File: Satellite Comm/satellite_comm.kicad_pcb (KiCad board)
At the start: 2 copper layers, 139.7 x 100.3 mm, 9 parts, among them J1 PC104_40Pin_2.54mm, J2 RockBLOCK9603, U1 SAM-M8Q

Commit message: Deleted all caches and renamed files...
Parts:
- removed J2: RockBLOCK9603, Molex_533981071:Molex_53398-1071
- removed U1: SAM-M8Q, SAMM8Q:SAM-M8Q
- removed XB1: XBee, WhitworthStandard:xbee-standard
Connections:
- J1 pad 1: GND -> +5V
- J1 pad 10: /I2C_SCL -> /IRIDIUM_NET_AVAIL
- J1 pad 11: /I2C_SDA -> GNDS
- J1 pad 12: GNDS -> /POD_RX
- J1 pad 13: /DIO1 -> /POD_TX
- J1 pad 14: /SPI_CLK -> /POD_WAKE
- J1 pad 15: /SPI_MISO -> /A3
- J1 pad 16: /SPI_MOSI -> /A4
- J1 pad 17: GND -> GNDPWR
- J1 pad 19: +3V3 -> +BATT
- J1 pad 2: /EXT_TEMP -> /SPI_MOSI
- J1 pad 20: GND -> +3V3
- J1 pad 21: +3V3 -> GND
- J1 pad 22: +3V3 -> +BATT
- J1 pad 24: /RADIO_WAKE -> /LED_A
- J1 pad 25: /1_WIRE -> /LED_B
- J1 pad 26: /IRIDIUM_NET_AVAIL -> /LED_C
- J1 pad 27: /IRIDIUM_TX -> /A0
- J1 pad 28: /IRIDIUM_RX -> /A1
- J1 pad 29: /IRIDIUM_PWR_CTRL -> /A2
- J1 pad 3: /A3 -> /SPI_MISO
- J1 pad 30: /INTERBOARD_0 -> /AUDIO_ALERT
- J1 pad 31: /INTERBOARD_1 -> /PWM
- J1 pad 32: /INTERBOARD_2 -> /DIO1
- J1 pad 33: /INTERBOARD_3 -> /INTERBOARD_0
- J1 pad 34: /PWM -> /RADIO_TX
- J1 pad 35: /LED_C -> /RADIO_RX
- J1 pad 36: /LED_B -> /RADIO_WAKE
- J1 pad 37: /LED_A -> /I2C_SDA
- J1 pad 38: /RADIO_RX -> /BT_RX
- J1 pad 39: /RADIO_TX -> /BT_TX
- J1 pad 4: /A2 -> /SPI_CLK
- J1 pad 40: +5V -> GND
- J1 pad 5: /A1 -> /I2C_SCL
- J1 pad 6: /A0 -> /DIO2
- J1 pad 7: /POD_WAKE -> /IRIDIUM_PWR_CTRL
- J1 pad 8: /POD_TX -> /IRIDIUM_RX
- J1 pad 9: /POD_RX -> /IRIDIUM_TX
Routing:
- net GND: track 0.00 -> 277.1 mm
- net +BATT: track 0.00 -> 2.54 mm
- net +3V3: track 2.54 -> 0.00 mm
- added copper zone on B.Cu, net GND
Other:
- board text added: "High Altitude Balloon Command Module 2.0 Processing Board"
- board text removed: "High Altitude Balloon Command Module 2.1 Processing Board"

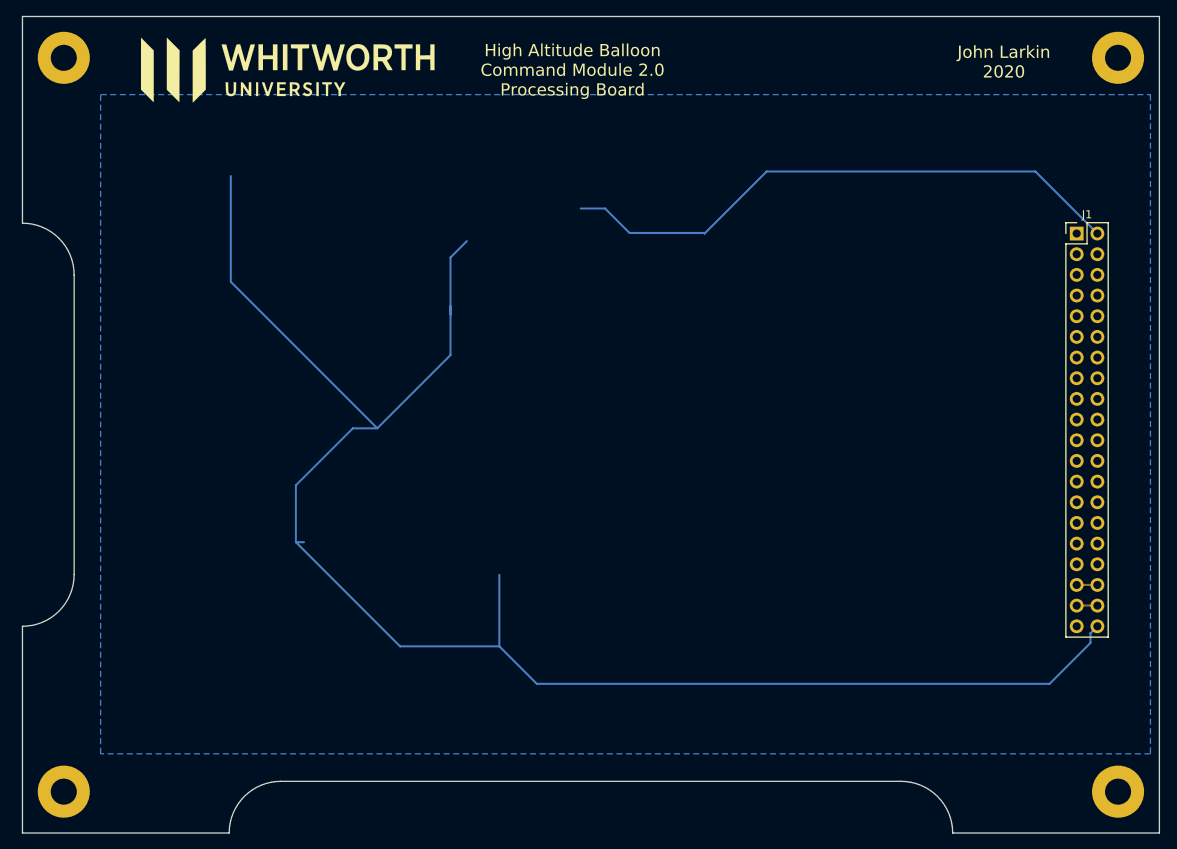
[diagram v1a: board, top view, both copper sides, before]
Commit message: silks are not very clean, laid out components, added front ground plane
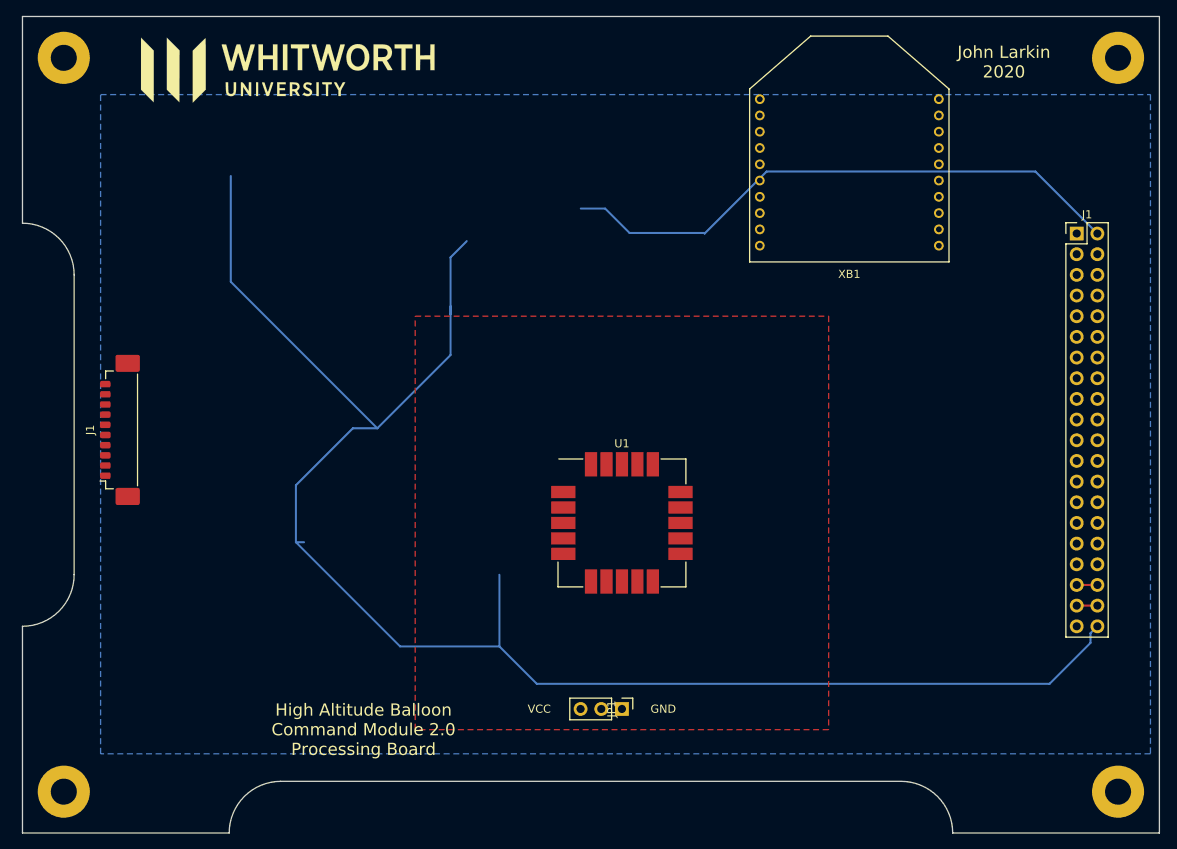
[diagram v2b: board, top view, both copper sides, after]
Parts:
- added J1: RockBlock Connector, Connector_Molex:Molex_PicoBlade_53398-1071_1x10-1MP_P1.25mm_Vertical, F.Cu at (36.8, 76.2)
- added JP1: Jumper_3_Open, Connector_PinHeader_2.54mm:PinHeader_1x03_P2.54mm_Vertical, F.Cu at (99.1, 110.5)
- added U1: SAM-M8Q, RF_GPS:ublox_SAM-M8Q_HandSolder, F.Cu at (99.1, 87.6)
- added XB1: XBee, WhitworthStandard:xbee-standard, F.Cu at (127.0, 35.6)
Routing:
- added copper zone on F.Cu, net GND
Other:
- board text added: "GND"
- board text added: "VCC"

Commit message: started working on tracks
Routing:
- net GND: track 277.1 -> 32.3 mm
- net +3V3: track 0.00 -> 187.4 mm, vias 0 -> 3
- net Net-(JP1-Pad2): track 0.00 -> 47.4 mm, vias 0 -> 1
- removed copper zone on B.Cu, net GND
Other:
- board text added: "Pin 1"

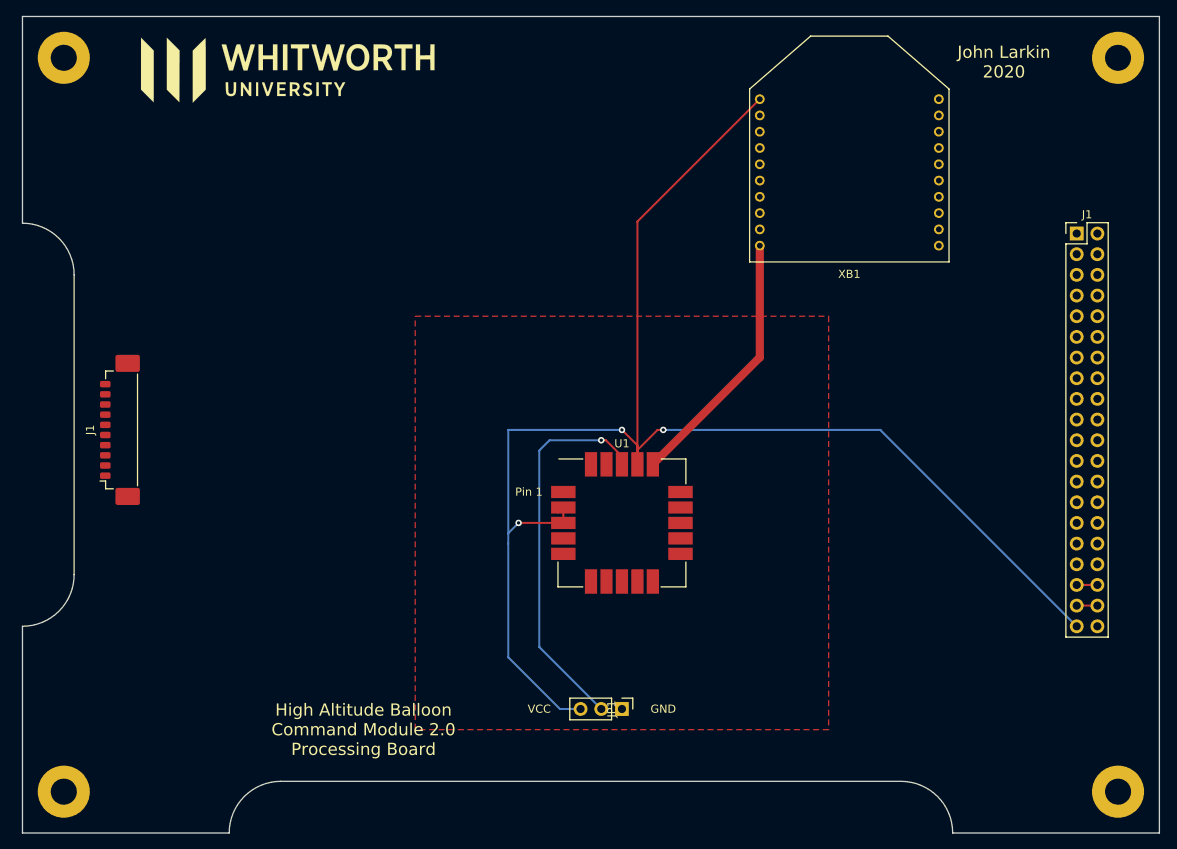
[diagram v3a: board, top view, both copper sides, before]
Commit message: made a couple more changes- switched out through board connector bc J1 had all pins wrong. placed j2 precisely over j1 and deleted j1
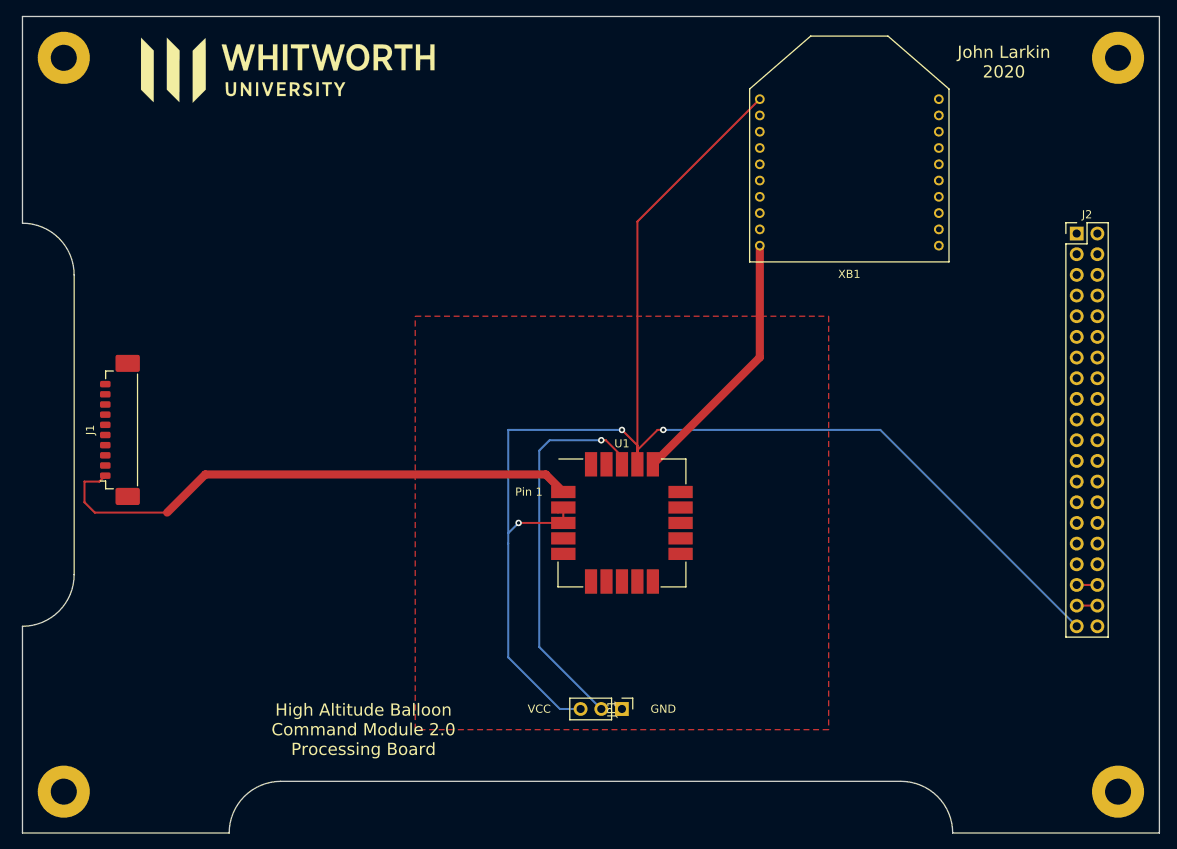
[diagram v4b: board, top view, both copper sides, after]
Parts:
- removed the J1 at (154.9, 52.1)
- added J2: PC104_40Pin_2.54mm-WhitworthStandard, WhitworthStandard:PC104_40PinSocket_2.54mm, F.Cu at (154.9, 52.1)
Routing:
- net GND: track 32.3 -> 99.9 mm
- net +BATT: track 2.54 -> 0.00 mm
- net +3V3: track 187.4 -> 190.0 mm

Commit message: routed all tracks... may want to move some of the ones coming from J1
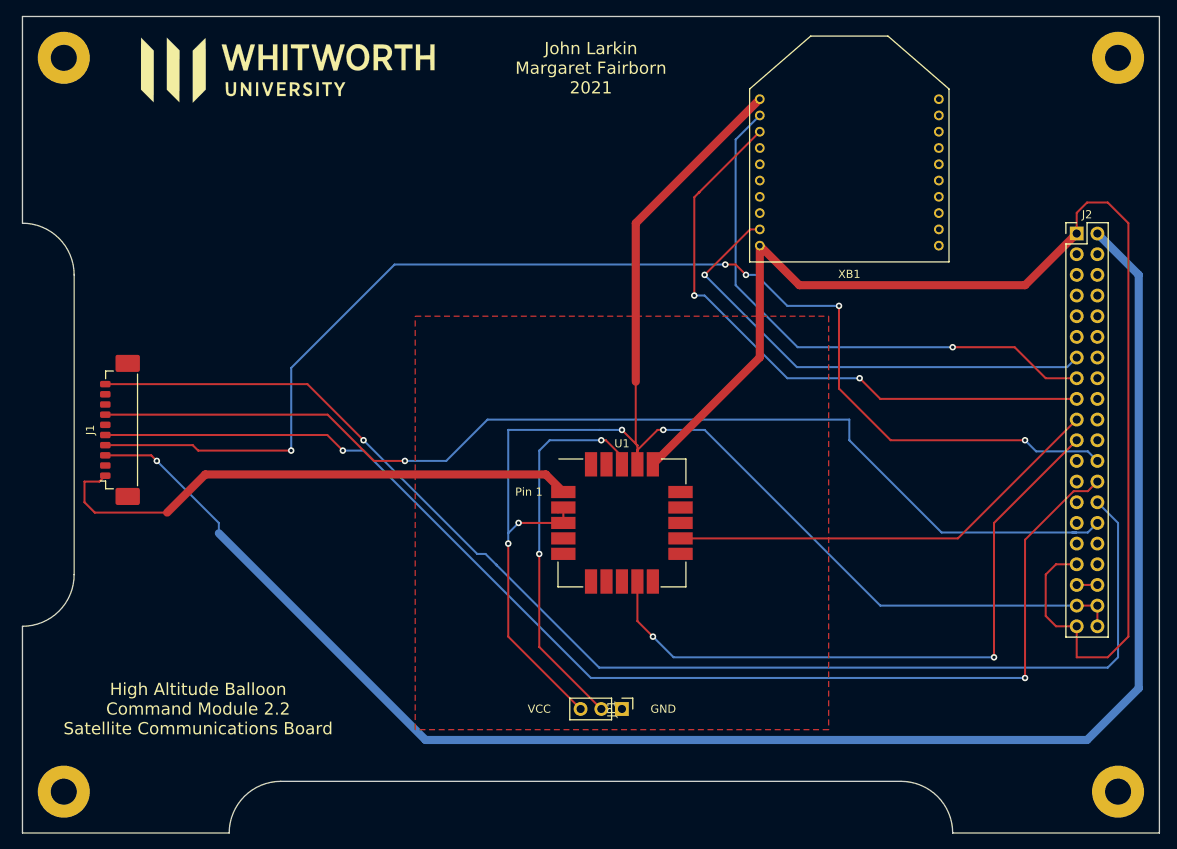
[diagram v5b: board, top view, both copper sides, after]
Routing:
- net +5V: track 0.00 -> 202.8 mm, vias 0 -> 1
- net /IRIDIUM_TX: track 0.00 -> 159.7 mm, vias 0 -> 1
- net /IRIDIUM_RX: track 0.00 -> 154.2 mm, vias 0 -> 2
- net /IRIDIUM_PWR_CTRL: track 0.00 -> 153.5 mm, vias 0 -> 5
- net /IRIDIUM_NET_AVAIL: track 0.00 -> 134.5 mm, vias 0 -> 1
- net GND: track 99.9 -> 229.7 mm
- net /I2C_SDA: track 0.00 -> 81.4 mm, vias 0 -> 2
- net /POD_RX: track 0.00 -> 75.8 mm, vias 0 -> 2
- net /POD_TX: track 0.00 -> 68.7 mm, vias 0 -> 1
- net /POD_WAKE: track 0.00 -> 60.0 mm, vias 0 -> 1
- net /I2C_SCL: track 0.00 -> 54.7 mm
- net +3V3: track 190.0 -> 187.8 mm, vias 3 -> 4
- net Net-(JP1-Pad2): vias 1 -> 2
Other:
- board text added: "High Altitude Balloon Command Module 2.2 Satellite Communications Board"
- board text added: "John Larkin Margaret Fairborn 2021"
- board text added: "placed j2 exactly over old j1 and deleted old j1 because old j1 had all the wrong tracks"
- board text removed: "High Altitude Balloon Command Module 2.0 Processing Board"
- board text removed: "John Larkin 2020"
